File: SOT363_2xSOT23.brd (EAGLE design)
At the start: 9 parts

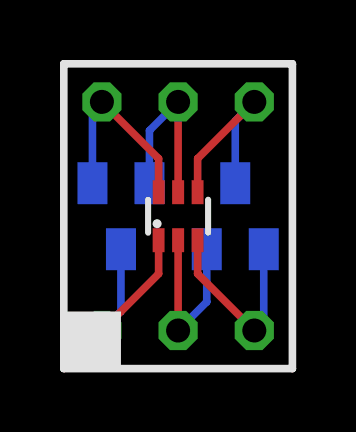
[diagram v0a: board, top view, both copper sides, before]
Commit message: adjusted trace widths
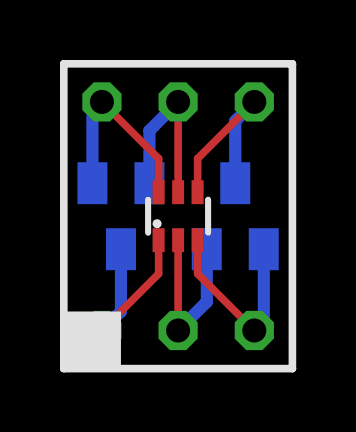
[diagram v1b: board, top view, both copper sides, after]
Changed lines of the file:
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@@
 <grid distance="0.05" unitdist="inch" unit="mm" style="lines" multiple="1" display="yes" altdistance="0.025" altunitdist="inch" altunit="mm"/>
 <layers>
-<layer number="1" name="Top" color="4" fill="1" visible="yes" active="yes"/>
+<layer number="1" name="Top" color="4" fill="1" visible="no" active="yes"/>
 <layer number="2" name="Route2" color="1" fill="3" visible="no" active="no"/>
 <layer number="3" name="Route3" color="4" fill="3" visible="no" active="no"/>
@@
 <layer number="19" name="Unrouted" color="6" fill="1" visible="yes" active="yes"/>
 <layer number="20" name="Dimension" color="15" fill="1" visible="yes" active="yes"/>
-<layer number="21" name="tPlace" color="7" fill="1" visible="yes" active="yes"/>
+<layer number="21" name="tPlace" color="7" fill="1" visible="no" active="yes"/>
 <layer number="22" name="bPlace" color="7" fill="1" visible="yes" active="yes"/>
-<layer number="23" name="tOrigins" color="15" fill="1" visible="yes" active="yes"/>
+<layer number="23" name="tOrigins" color="15" fill="1" visible="no" active="yes"/>
 <layer number="24" name="bOrigins" color="15" fill="1" visible="yes" active="yes"/>
-<layer number="25" name="tNames" color="7" fill="1" visible="yes" active="yes"/>
+<layer number="25" name="tNames" color="7" fill="1" visible="no" active="yes"/>
 <layer number="26" name="bNames" color="7" fill="1" visible="yes" active="yes"/>
-<layer number="27" name="tValues" color="7" fill="1" visible="yes" active="yes"/>
-<layer number="28" name="bValues" color="7" fill="1" visible="yes" active="yes"/>
+<layer number="27" name="tValues" color="7" fill="1" visible="no" active="yes"/>
+<layer number="28" name="bValues" color="7" fill="1" visible="no" active="yes"/>
 <layer number="29" name="tStop" color="7" fill="3" visible="no" active="yes"/>
-<layer number="30" name="bStop" color="7" fill="6" visible="no" active="yes"/>
+<layer number="30" name="bStop" color="7" fill="6" visible="yes" active="yes"/>
 <layer number="31" name="tCream" color="7" fill="4" visible="no" active="yes"/>
 <layer number="32" name="bCream" color="7" fill="5" visible="no" active="yes"/>
@@
 <layer number="37" name="tTest" color="7" fill="1" visible="no" active="yes"/>
 <layer number="38" name="bTest" color="7" fill="1" visible="no" active="yes"/>
-<layer number="39" name="tKeepout" color="4" fill="11" visible="yes" active="yes"/>
+<layer number="39" name="tKeepout" color="4" fill="11" visible="no" active="yes"/>
 <layer number="40" name="bKeepout" color="1" fill="11" visible="yes" active="yes"/>
-<layer number="41" name="tRestrict" color="4" fill="10" visible="yes" active="yes"/>
+<layer number="41" name="tRestrict" color="4" fill="10" visible="no" active="yes"/>
 <layer number="42" name="bRestrict" color="1" fill="10" visible="yes" active="yes"/>
 <layer number="43" name="vRestrict" color="2" fill="10" visible="yes" active="yes"/>
 <layer number="44" name="Drills" color="7" fill="1" visible="no" active="yes"/>
 <layer number="45" name="Holes" color="7" fill="1" visible="no" active="yes"/>
-<layer number="46" name="Milling" color="3" fill="1" visible="no" active="yes"/>
+<layer number="46" name="Milling" color="3" fill="1" visible="yes" active="yes"/>
 <layer number="47" name="Measures" color="7" fill="1" visible="no" active="yes"/>
-<layer number="48" name="Document" color="7" fill="1" visible="yes" active="yes"/>
-<layer number="49" name="Reference" color="7" fill="1" visible="yes" active="yes"/>
-<layer number="51" name="tDocu" color="7" fill="1" visible="yes" active="yes"/>
-<layer number="52" name="bDocu" color="7" fill="1" visible="yes" active="yes"/>
+<layer number="48" name="Document" color="7" fill="1" visible="no" active="yes"/>
+<layer number="49" name="Reference" color="7" fill="1" visible="no" active="yes"/>
+<layer number="51" name="tDocu" color="7" fill="1" visible="no" active="yes"/>
+<layer number="52" name="bDocu" color="7" fill="1" visible="no" active="yes"/>
 <layer number="91" name="Nets" color="2" fill="1" visible="no" active="no"/>
 <layer number="92" name="Busses" color="1" fill="1" visible="no" active="no"/>
@@
 <layer number="97" name="Info" color="7" fill="1" visible="no" active="no"/>
 <layer number="98" name="Guide" color="6" fill="1" visible="no" active="no"/>
-<layer number="125" name="_tNames" color="14" fill="1" visible="yes" active="yes"/>
-<layer number="126" name="_bNames" color="5" fill="1" visible="yes" active="yes"/>
+<layer number="125" name="_tNames" color="14" fill="1" visible="no" active="yes"/>
+<layer number="126" name="_bNames" color="5" fill="1" visible="no" active="yes"/>
 <layer number="200" name="200bmp" color="1" fill="10" visible="no" active="no"/>
 </layers>
@@
 <contactref element="E$619" pad="P$1"/>
 <contactref element="E$622" pad="3"/>
-<wire x1="1.905" y1="3.98" x2="1.905" y2="1.905" width="0.254" layer="16"/>
-<wire x1="1.905" y1="1.905" x2="1.27" y2="1.27" width="0.254" layer="16"/>
+<wire x1="1.905" y1="3.98" x2="1.905" y2="1.905" width="0.4064" layer="16"/>
+<wire x1="1.905" y1="1.905" x2="1.27" y2="1.27" width="0.4064" layer="16"/>
 <contactref element="E$614" pad="1"/>
 <wire x1="3.16" y1="4.28" x2="3.16" y2="3.16" width="0.254" layer="1"/>
@@
 <contactref element="E$620" pad="P$1"/>
 <contactref element="E$623" pad="2"/>
-<wire x1="4.765" y1="3.98" x2="4.765" y2="2.225" width="0.254" layer="16"/>
-<wire x1="4.765" y1="2.225" x2="3.81" y2="1.27" width="0.254" layer="16"/>
+<wire x1="4.765" y1="3.98" x2="4.765" y2="2.225" width="0.4064" layer="16"/>
+<wire x1="4.765" y1="2.225" x2="3.81" y2="1.27" width="0.4064" layer="16"/>
 <contactref element="E$614" pad="2"/>
 <wire x1="3.81" y1="4.28" x2="3.81" y2="1.27" width="0.254" layer="1"/>
@@
 <contactref element="E$621" pad="P$1"/>
 <contactref element="E$623" pad="1"/>
-<wire x1="6.665" y1="3.98" x2="6.665" y2="1.585" width="0.254" layer="16"/>
-<wire x1="6.665" y1="1.585" x2="6.35" y2="1.27" width="0.254" layer="16"/>
+<wire x1="6.665" y1="3.98" x2="6.665" y2="1.585" width="0.4064" layer="16"/>
+<wire x1="6.665" y1="1.585" x2="6.35" y2="1.27" width="0.4064" layer="16"/>
 <contactref element="E$614" pad="3"/>
 <wire x1="4.46" y1="4.28" x2="4.46" y2="3.16" width="0.254" layer="1"/>
@@
 <contactref element="E$618" pad="P$1"/>
 <contactref element="E$623" pad="3"/>
-<wire x1="5.715" y1="6.18" x2="5.715" y2="8.255" width="0.254" layer="16"/>
-<wire x1="5.715" y1="8.255" x2="6.35" y2="8.89" width="0.254" layer="16"/>
+<wire x1="5.715" y1="6.18" x2="5.715" y2="8.255" width="0.4064" layer="16"/>
+<wire x1="5.715" y1="8.255" x2="6.35" y2="8.89" width="0.4064" layer="16"/>
 <contactref element="E$614" pad="4"/>
 <wire x1="4.46" y1="5.88" x2="4.46" y2="7" width="0.254" layer="1"/>
@@
 <contactref element="E$617" pad="P$1"/>
 <contactref element="E$622" pad="2"/>
-<wire x1="2.855" y1="6.18" x2="2.855" y2="7.935" width="0.254" layer="16"/>
-<wire x1="2.855" y1="7.935" x2="3.81" y2="8.89" width="0.254" layer="16"/>
+<wire x1="2.855" y1="6.18" x2="2.855" y2="7.935" width="0.4064" layer="16"/>
+<wire x1="2.855" y1="7.935" x2="3.81" y2="8.89" width="0.4064" layer="16"/>
 <contactref element="E$614" pad="5"/>
 <wire x1="3.81" y1="5.88" x2="3.81" y2="8.89" width="0.254" layer="1"/>
@@
 <contactref element="E$616" pad="P$1"/>
 <contactref element="E$622" pad="1"/>
-<wire x1="0.955" y1="6.18" x2="0.955" y2="8.575" width="0.254" layer="16"/>
-<wire x1="0.955" y1="8.575" x2="1.27" y2="8.89" width="0.254" layer="16"/>
+<wire x1="0.955" y1="6.18" x2="0.955" y2="8.575" width="0.4064" layer="16"/>
+<wire x1="0.955" y1="8.575" x2="1.27" y2="8.89" width="0.4064" layer="16"/>
 <contactref element="E$614" pad="6"/>
 <wire x1="3.16" y1="5.88" x2="3.16" y2="7" width="0.254" layer="1"/>
